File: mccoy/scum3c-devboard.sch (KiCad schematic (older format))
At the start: 26 parts, among them J1 Conn_02x10_Odd_Even, J2 Conn_02x10_Odd_Even, J3 Conn_02x05_Odd_Even, J4 Conn_01x01_Male, U9AB1 ICM-20948

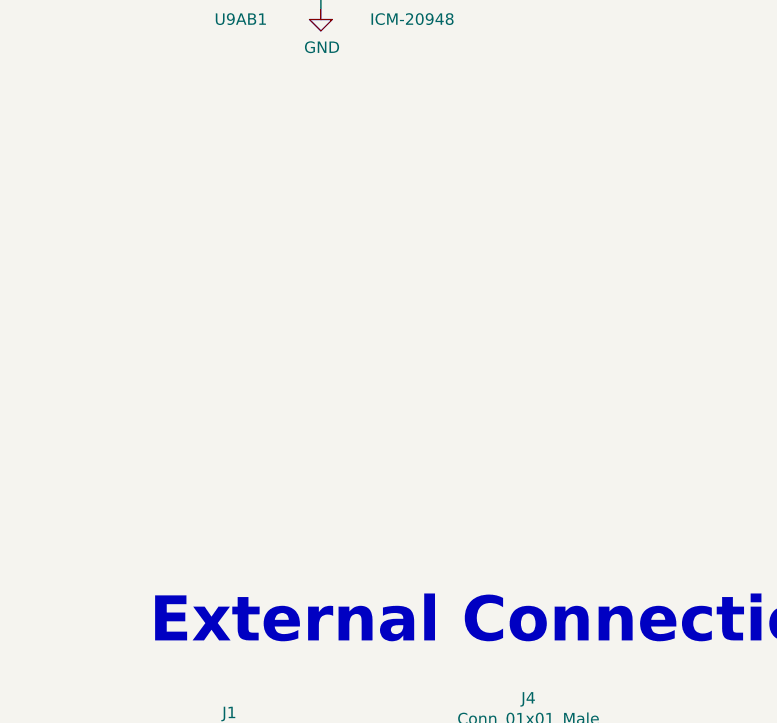
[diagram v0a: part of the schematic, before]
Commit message: assigned most footprints
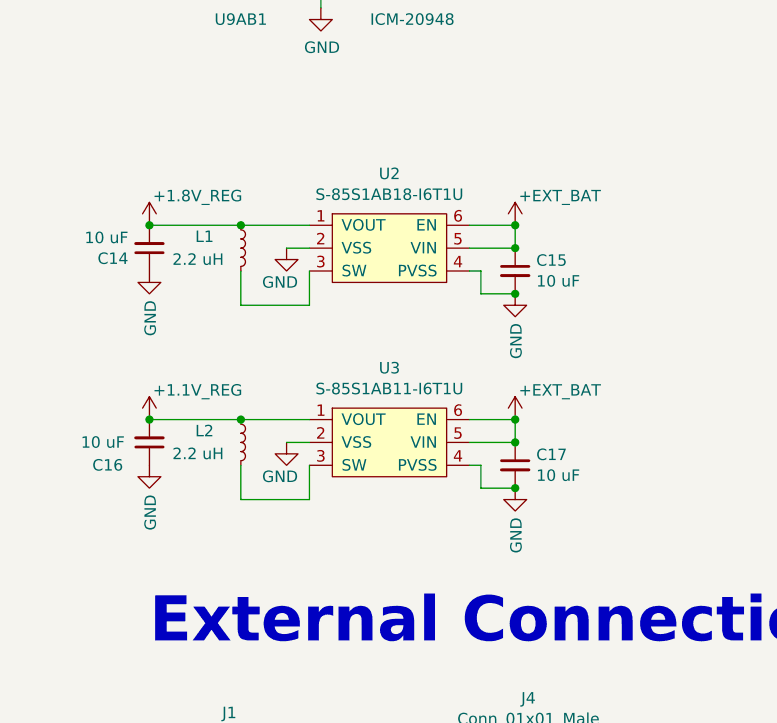
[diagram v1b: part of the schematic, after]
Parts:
- added C14, C15, C16, C17: 10 uF, symbol Device:C_Small
- added L1, L2: 2.2 uH, symbol Device:L_Small
- added U2: S-85S1AB18-I6T1U, symbol draft1library:S-85S1AB18-I6T1U
- added U3: S-85S1AB11-I6T1U, symbol draft1library:S-85S1AB11-I6T1U
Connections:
- wire segments 23 -> 47

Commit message: created snt-6a footprint
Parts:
- BT1: footprint SamacSys_Parts:2986 -> Battery:Battery_Panasonic_CR2032-VS1N_Vertical_CircularHoles
- C14, C15, C16, C17: footprint (none) -> Capacitor_SMD:C_0402_1005Metric
- J1: footprint (none) -> Connector_PinHeader_2.54mm:PinHeader_2x10_P2.54mm_Vertical
- J3: footprint (none) -> Connector_PinHeader_2.54mm:PinHeader_2x05_P2.54mm_Vertical
- L1, L2: footprint (none) -> Inductor_SMD:L_0402_1005Metric
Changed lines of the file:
@@
 F 0 "BT1" H 10000 1846 50  0000 L CNN
 F 1 "Battery_Clip" H 10000 1755 50  0000 L CNN
-F 2 "SamacSys_Parts:2986" H 9800 1750 50  0001 C CNN
+F 2 "Battery:Battery_Panasonic_CR2032-VS1N_Vertical_CircularHoles" H 9800 1750 50  0001 C CNN
 F 3 "" H 9800 1750 50  0001 C CNN
 	1    9800 1750
@@
 F 0 "J1" H 1400 7717 50  0000 C CNN
 F 1 "Conn_02x10_Odd_Even" H 1400 7626 50  0000 C CNN
-F 2 "" H 1350 7100 50  0001 C CNN
+F 2 "Connector_PinHeader_2.54mm:PinHeader_2x10_P2.54mm_Vertical" H 1350 7100 50  0001 C CNN
 F 3 "~" H 1350 7100 50  0001 C CNN
 	1    1350 7100
@@
 F 0 "J3" H 5200 7367 50  0000 C CNN
 F 1 "Conn_02x05_Odd_Even" H 5200 7276 50  0000 C CNN
-F 2 "" H 5150 6950 50  0001 C CNN
+F 2 "Connector_PinHeader_2.54mm:PinHeader_2x05_P2.54mm_Vertical" H 5150 6950 50  0001 C CNN
 F 3 "~" H 5150 6950 50  0001 C CNN
 	1    5150 6950
@@
 F 0 "C14" H 1142 4496 50  0000 L CNN
 F 1 "10 uF" H 1142 4405 50  0000 L CNN
-F 2 "" H 1050 4450 50  0001 C CNN
+F 2 "Capacitor_SMD:C_0402_1005Metric" H 1050 4450 50  0001 C CNN
 F 3 "~" H 1050 4450 50  0001 C CNN
 	1    1050 4450
@@
 F 0 "L1" H 1250 4500 50  0000 L CNN
 F 1 "2.2 uH" H 1150 4400 50  0000 L CNN
-F 2 "" H 1450 4450 50  0001 C CNN
+F 2 "Inductor_SMD:L_0402_1005Metric" H 1450 4450 50  0001 C CNN
 F 3 "~" H 1450 4450 50  0001 C CNN
 	1    1450 4450
@@
 F 0 "C16" H 1300 5400 50  0000 R CNN
 F 1 "10 uF" H 1350 5300 50  0000 R CNN
-F 2 "" H 1050 5300 50  0001 C CNN
+F 2 "Capacitor_SMD:C_0402_1005Metric" H 1050 5300 50  0001 C CNN
 F 3 "~" H 1050 5300 50  0001 C CNN
 	1    1050 5300
@@
 F 0 "L2" H 1250 5350 50  0000 L CNN
 F 1 "2.2 uH" H 1150 5250 50  0000 L CNN
-F 2 "" H 1450 5300 50  0001 C CNN
+F 2 "Inductor_SMD:L_0402_1005Metric" H 1450 5300 50  0001 C CNN
 F 3 "~" H 1450 5300 50  0001 C CNN
 	1    1450 5300
@@
 F 0 "C17" H 2742 5446 50  0000 L CNN
 F 1 "10 uF" H 2742 5355 50  0000 L CNN
-F 2 "" H 2650 5400 50  0001 C CNN
+F 2 "Capacitor_SMD:C_0402_1005Metric" H 2650 5400 50  0001 C CNN
 F 3 "~" H 2650 5400 50  0001 C CNN
 	1    2650 5400
@@
 F 0 "C15" H 2742 4596 50  0000 L CNN
 F 1 "10 uF" H 2742 4505 50  0000 L CNN
-F 2 "" H 2650 4550 50  0001 C CNN
+F 2 "Capacitor_SMD:C_0402_1005Metric" H 2650 4550 50  0001 C CNN
 F 3 "~" H 2650 4550 50  0001 C CNN
 	1    2650 4550

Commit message: added regulators to pcb
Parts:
- removed BT1: Battery_Clip, Battery:Battery_Panasonic_CR2032-VS1N_Vertical_CircularHoles, symbol draft1library:Battery_Clip
- added BT1: Battery_Cell, Battery:Battery_Panasonic_CR2032-VS1N_Vertical_CircularHoles, symbol Device:Battery_Cell
- U2, U3: footprint (none) -> SCUM:SNT-6A
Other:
- note added: "Regulators"
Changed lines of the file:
@@
 	1    0    0    -1
-$EndComp
-$Comp
-L draft1library:+VBAT #PWR047
-U 1 1 607B4D72
-P 9800 2050
-F 0 "#PWR047" H 9800 1900 50  0001 C CNN
-F 1 "+VBAT" H 9815 2223 50  0000 C CNN
-F 2 "" H 9800 2050 50  0001 C CNN
-F 3 "" H 9800 2050 50  0001 C CNN
-	1    9800 2050
-	-1   0    0    1
 $EndComp
 $Sheet
@@
 $EndSheet
 $Comp
-L draft1library:Battery_Clip BT1
-U 1 1 60775F67
-P 9800 1750
-F 0 "BT1" H 10000 1846 50  0000 L CNN
-F 1 "Battery_Clip" H 10000 1755 50  0000 L CNN
-F 2 "Battery:Battery_Panasonic_CR2032-VS1N_Vertical_CircularHoles" H 9800 1750 50  0001 C CNN
-F 3 "" H 9800 1750 50  0001 C CNN
-	1    9800 1750
-	1    0    0    -1
-$EndComp
-$Comp
 L draft1library:+VBAT #PWR048
 U 1 1 608BF8E8
-P 9850 1350
-F 0 "#PWR048" H 9850 1200 50  0001 C CNN
-F 1 "+VBAT" H 9865 1523 50  0000 C CNN
-F 2 "" H 9850 1350 50  0001 C CNN
-F 3 "" H 9850 1350 50  0001 C CNN
-	1    9850 1350
+P 9850 1650
+F 0 "#PWR048" H 9850 1500 50  0001 C CNN
+F 1 "+VBAT" H 9865 1823 50  0000 C CNN
+F 2 "" H 9850 1650 50  0001 C CNN
+F 3 "" H 9850 1650 50  0001 C CNN
+	1    9850 1650
 	1    0    0    -1
 $EndComp
@@
 L power:GND #PWR046
 U 1 1 608BFCDC
-P 9750 1350
+P 9850 2000
 AR Path="/608BFCDC" Ref="#PWR046"  Part="1"
 AR Path="/5F3B0B28/608BFCDC" Ref="#PWR?"  Part="1"
-F 0 "#PWR046" H 9750 1100 50  0001 C CNN
-F 1 "GND" H 9755 1177 50  0000 C CNN
-F 2 "" H 9750 1350 50  0001 C CNN
-F 3 "" H 9750 1350 50  0001 C CNN
-	1    9750 1350
-	-1   0    0    1
+F 0 "#PWR046" H 9850 1750 50  0001 C CNN
+F 1 "GND" H 9855 1827 50  0000 C CNN
+F 2 "" H 9850 2000 50  0001 C CNN
+F 3 "" H 9850 2000 50  0001 C CNN
+	1    9850 2000
+	1    0    0    -1
 $EndComp
 $Comp
@@
 F 0 "U3" H 2100 5625 50  0000 C CNN
 F 1 "S-85S1AB11-I6T1U" H 2100 5534 50  0000 C CNN
-F 2 "" H 2300 5200 50  0001 C CNN
+F 2 "SCUM:SNT-6A" H 2300 5200 50  0001 C CNN
 F 3 "" H 2300 5200 50  0001 C CNN
 	1    2100 5300
@@
 F 0 "U2" H 2100 4775 50  0000 C CNN
 F 1 "S-85S1AB18-I6T1U" H 2100 4684 50  0000 C CNN
-F 2 "" H 2300 4350 50  0001 C CNN
+F 2 "SCUM:SNT-6A" H 2300 4350 50  0001 C CNN
 F 3 "" H 2300 4350 50  0001 C CNN
 	1    2100 4450
@@
 	1    0    0    -1
 $EndComp
+$Comp
+L Device:Battery_Cell BT1
+U 1 1 612886A9
+P 9850 1850
+F 0 "BT1" H 9968 1946 50  0000 L CNN
+F 1 "Battery_Cell" H 9968 1855 50  0000 L CNN
+F 2 "Battery:Battery_Panasonic_CR2032-VS1N_Vertical_CircularHoles" V 9850 1910 50  0001 C CNN
+F 3 "~" V 9850 1910 50  0001 C CNN
+	1    9850 1850
+	1    0    0    -1
+$EndComp
+Text Notes 1050 4000 0    197  ~ 39
+Regulators
 $EndSCHEMATC

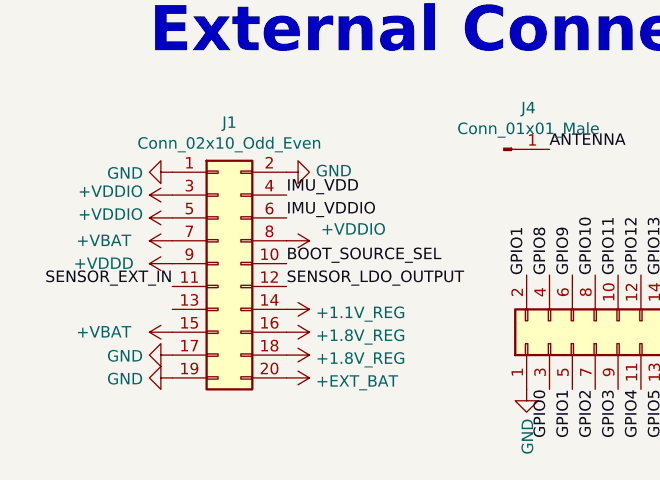
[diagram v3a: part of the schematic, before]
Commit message: moved pins for better tracing
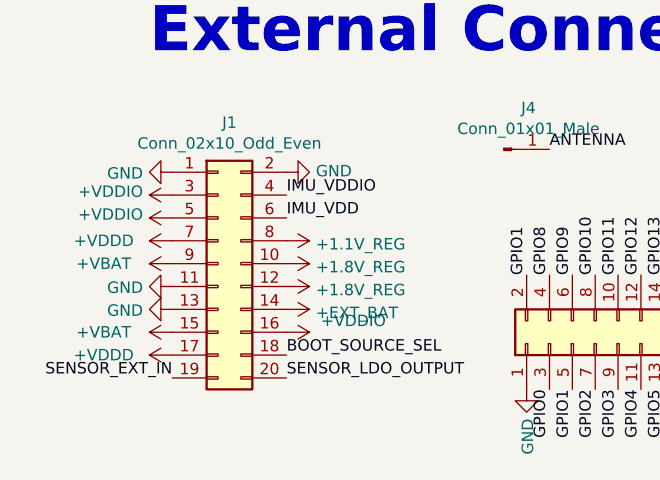
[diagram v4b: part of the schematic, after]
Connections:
- net +1.1V_REG: now also J1.8 (Pin_8); no longer J1.14 (Pin_14)
- net +1.8V_REG: now also J1.10 (Pin_10), J1.12 (Pin_12); no longer J1.16 (Pin_16), J1.18 (Pin_18)
- net +EXT_BAT: now also J1.14 (Pin_14); no longer J1.20 (Pin_20)
- net +VBAT: now also J1.9 (Pin_9); no longer J1.7 (Pin_7)
- net +VDDD: now also J1.17 (Pin_17), J1.7 (Pin_7); no longer J1.9 (Pin_9)
- net +VDDIO: now also J1.16 (Pin_16); no longer J1.8 (Pin_8)
- net BOOT_SOURCE_SEL: now also J1.18 (Pin_18); no longer J1.10 (Pin_10)
- net GND: now also J1.11 (Pin_11), J1.13 (Pin_13); no longer J1.17 (Pin_17), J1.19 (Pin_19)
- net IMU_VDD: now also J1.6 (Pin_6); no longer J1.4 (Pin_4)
- net IMU_VDDIO: now also J1.4 (Pin_4); no longer J1.6 (Pin_6)
- net SENSOR_EXT_IN: now also J1.19 (Pin_19); no longer J1.11 (Pin_11)
- net SENSOR_LDO_OUTPUT: now also J1.20 (Pin_20); no longer J1.12 (Pin_12)
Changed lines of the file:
@@
 Text Label 1700 1750 2    50   ~ 0
 IMU_VDDIO
-Text Label 1650 6900 0    50   ~ 0
+Text Label 1650 6800 0    50   ~ 0
 IMU_VDDIO
 Text Label 3200 7150 1    50   ~ 0
@@
 Text Label 3500 7150 1    50   ~ 0
 GPIO15
-Text Label 1650 6800 0    50   ~ 0
+Text Label 1650 6900 0    50   ~ 0
 IMU_VDD
 NoConn ~ 1300 2950
@@
 	0    1    1    0
 $EndComp
-Text Label 1650 7100 0    50   ~ 0
+Text Label 1650 7500 0    50   ~ 0
 BOOT_SOURCE_SEL
 Text Label 5450 7150 0    50   ~ 0
@@
 	0    1    1    0
 $EndComp
-$Comp
-L draft1library:+VDDD #PWR07
-U 1 1 60769F1D
-P 1150 7100
-F 0 "#PWR07" H 1150 6950 50  0001 C CNN
-F 1 "+VDDD" V 1150 7400 50  0000 C CNN
-F 2 "" H 1150 7100 50  0001 C CNN
-F 3 "" H 1150 7100 50  0001 C CNN
-	1    1150 7100
-	0    -1   -1   0
-$EndComp
-Text Label 1150 7200 2    50   ~ 0
+Text Label 1150 7600 2    50   ~ 0
 SENSOR_EXT_IN
-Text Label 1650 7200 0    50   ~ 0
+Text Label 1650 7600 0    50   ~ 0
 SENSOR_LDO_OUTPUT
 Text Label 4950 6950 2    50   ~ 0
@@
 L draft1library:+VBAT #PWR?
 U 1 1 6076D7B9
-P 1150 7000
+P 1150 7400
 AR Path="/5F3B1D81/6076D7B9" Ref="#PWR?"  Part="1"
 AR Path="/5F41418C/6076D7B9" Ref="#PWR?"  Part="1"
 AR Path="/5F414989/6076D7B9" Ref="#PWR?"  Part="1"
 AR Path="/6076D7B9" Ref="#PWR06"  Part="1"
-F 0 "#PWR06" H 1150 6850 50  0001 C CNN
-F 1 "+VBAT" V 1150 7300 50  0000 C CNN
-F 2 "" H 1150 7000 50  0001 C CNN
-F 3 "" H 1150 7000 50  0001 C CNN
-	1    1150 7000
+F 0 "#PWR06" H 1150 7250 50  0001 C CNN
+F 1 "+VBAT" V 1150 7700 50  0000 C CNN
+F 2 "" H 1150 7400 50  0001 C CNN
+F 3 "" H 1150 7400 50  0001 C CNN
+	1    1150 7400
 	0    -1   -1   0
 $EndComp
@@
 F 3 "" H 1150 6700 50  0001 C CNN
 	1    1150 6700
-	0    1    1    0
-$EndComp
-$Comp
-L draft1library:+VDDIO #PWR?
-U 1 1 6076E794
-P 1650 7000
-AR Path="/5F3B1D81/6076E794" Ref="#PWR?"  Part="1"
-AR Path="/6076E794" Ref="#PWR08"  Part="1"
-F 0 "#PWR08" H 1650 6850 50  0001 C CNN
-F 1 "+VDDIO" V 1600 7150 50  0000 L CNN
-F 2 "" H 1650 7000 50  0001 C CNN
-F 3 "" H 1650 7000 50  0001 C CNN
-	1    1650 7000
 	0    1    1    0
 $EndComp
@@
 L draft1library:+VBAT #PWR?
 U 1 1 6127ADAC
-P 1150 7400
+P 1150 7100
 AR Path="/5F3B1D81/6127ADAC" Ref="#PWR?"  Part="1"
 AR Path="/5F41418C/6127ADAC" Ref="#PWR?"  Part="1"
 AR Path="/5F414989/6127ADAC" Ref="#PWR?"  Part="1"
 AR Path="/6127ADAC" Ref="#PWR0107"  Part="1"
-F 0 "#PWR0107" H 1150 7250 50  0001 C CNN
-F 1 "+VBAT" V 1150 7700 50  0000 C CNN
-F 2 "" H 1150 7400 50  0001 C CNN
-F 3 "" H 1150 7400 50  0001 C CNN
-	1    1150 7400
+F 0 "#PWR0107" H 1150 6950 50  0001 C CNN
+F 1 "+VBAT" V 1150 7400 50  0000 C CNN
+F 2 "" H 1150 7100 50  0001 C CNN
+F 3 "" H 1150 7100 50  0001 C CNN
+	1    1150 7100
 	0    -1   -1   0
 $EndComp
@@
 L power:GND #PWR0108
 U 1 1 6127B18B
-P 1150 7500
-F 0 "#PWR0108" H 1150 7250 50  0001 C CNN
-F 1 "GND" V 1155 7372 50  0000 R CNN
-F 2 "" H 1150 7500 50  0001 C CNN
-F 3 "" H 1150 7500 50  0001 C CNN
-	1    1150 7500
+P 1150 7200
+F 0 "#PWR0108" H 1150 6950 50  0001 C CNN
+F 1 "GND" V 1155 7072 50  0000 R CNN
+F 2 "" H 1150 7200 50  0001 C CNN
+F 3 "" H 1150 7200 50  0001 C CNN
+	1    1150 7200
 	0    1    1    0
 $EndComp
@@
 L power:GND #PWR0109
 U 1 1 6127B4FF
-P 1150 7600
-F 0 "#PWR0109" H 1150 7350 50  0001 C CNN
-F 1 "GND" V 1155 7472 50  0000 R CNN
-F 2 "" H 1150 7600 50  0001 C CNN
-F 3 "" H 1150 7600 50  0001 C CNN
-	1    1150 7600
+P 1150 7300
+F 0 "#PWR0109" H 1150 7050 50  0001 C CNN
+F 1 "GND" V 1155 7172 50  0000 R CNN
+F 2 "" H 1150 7300 50  0001 C CNN
+F 3 "" H 1150 7300 50  0001 C CNN
+	1    1150 7300
 	0    1    1    0
 $EndComp
@@
 L draft1library:+1.1V_REG #PWR0110
 U 1 1 61280E78
+P 1650 7000
+F 0 "#PWR0110" H 1650 6850 50  0001 C CNN
+F 1 "+1.1V_REG" V 1665 7128 50  0000 L CNN
+F 2 "" H 1650 7000 50  0001 C CNN
+F 3 "" H 1650 7000 50  0001 C CNN
+	1    1650 7000
+	0    1    1    0
+$EndComp
+$Comp
+L draft1library:+1.8V_REG #PWR0111
+U 1 1 61281B91
+P 1650 7100
+F 0 "#PWR0111" H 1650 6950 50  0001 C CNN
+F 1 "+1.8V_REG" V 1665 7228 50  0000 L CNN
+F 2 "" H 1650 7100 50  0001 C CNN
+F 3 "" H 1650 7100 50  0001 C CNN
+	1    1650 7100
+	0    1    1    0
+$EndComp
+$Comp
+L draft1library:+1.8V_REG #PWR0112
+U 1 1 612829BE
+P 1650 7200
+F 0 "#PWR0112" H 1650 7050 50  0001 C CNN
+F 1 "+1.8V_REG" V 1665 7328 50  0000 L CNN
+F 2 "" H 1650 7200 50  0001 C CNN
+F 3 "" H 1650 7200 50  0001 C CNN
+	1    1650 7200
+	0    1    1    0
+$EndComp
+$Comp
+L draft1library:+EXT_BAT #PWR0113
+U 1 1 612835E6
 P 1650 7300
-F 0 "#PWR0110" H 1650 7150 50  0001 C CNN
-F 1 "+1.1V_REG" V 1665 7428 50  0000 L CNN
+F 0 "#PWR0113" H 1650 7150 50  0001 C CNN
+F 1 "+EXT_BAT" V 1665 7428 50  0000 L CNN
 F 2 "" H 1650 7300 50  0001 C CNN
 F 3 "" H 1650 7300 50  0001 C CNN
 	1    1650 7300
-	0    1    1    0
-$EndComp
-$Comp
-L draft1library:+1.8V_REG #PWR0111
-U 1 1 61281B91
-P 1650 7400
-F 0 "#PWR0111" H 1650 7250 50  0001 C CNN
-F 1 "+1.8V_REG" V 1665 7528 50  0000 L CNN
-F 2 "" H 1650 7400 50  0001 C CNN
-F 3 "" H 1650 7400 50  0001 C CNN
-	1    1650 7400
-	0    1    1    0
-$EndComp
-$Comp
-L draft1library:+1.8V_REG #PWR0112
-U 1 1 612829BE
-P 1650 7500
-F 0 "#PWR0112" H 1650 7350 50  0001 C CNN
-F 1 "+1.8V_REG" V 1665 7628 50  0000 L CNN
-F 2 "" H 1650 7500 50  0001 C CNN
-F 3 "" H 1650 7500 50  0001 C CNN
-	1    1650 7500
-	0    1    1    0
-$EndComp
-$Comp
-L draft1library:+EXT_BAT #PWR0113
-U 1 1 612835E6
-P 1650 7600
-F 0 "#PWR0113" H 1650 7450 50  0001 C CNN
-F 1 "+EXT_BAT" V 1665 7728 50  0000 L CNN
-F 2 "" H 1650 7600 50  0001 C CNN
-F 3 "" H 1650 7600 50  0001 C CNN
-	1    1650 7600
 	0    1    1    0
 $EndComp
@@
 Text Notes 1050 4000 0    197  ~ 39
 Regulators
+$Comp
+L draft1library:+VDDD #PWR0125
+U 1 1 612C7D86
+P 1150 7000
+F 0 "#PWR0125" H 1150 6850 50  0001 C CNN
+F 1 "+VDDD" V 1150 7300 50  0000 C CNN
+F 2 "" H 1150 7000 50  0001 C CNN
+F 3 "" H 1150 7000 50  0001 C CNN
+	1    1150 7000
+	0    -1   -1   0
+$EndComp
+$Comp
+L draft1library:+VDDIO #PWR?
+U 1 1 6076E794
+P 1650 7400
+AR Path="/5F3B1D81/6076E794" Ref="#PWR?"  Part="1"
+AR Path="/6076E794" Ref="#PWR08"  Part="1"
+F 0 "#PWR08" H 1650 7250 50  0001 C CNN
+F 1 "+VDDIO" V 1600 7550 50  0000 L CNN
+F 2 "" H 1650 7400 50  0001 C CNN
+F 3 "" H 1650 7400 50  0001 C CNN
+	1    1650 7400
+	0    1    1    0
+$EndComp
+$Comp
+L draft1library:+VDDD #PWR07
+U 1 1 60769F1D
+P 1150 7500
+F 0 "#PWR07" H 1150 7350 50  0001 C CNN
+F 1 "+VDDD" V 1150 7800 50  0000 C CNN
+F 2 "" H 1150 7500 50  0001 C CNN
+F 3 "" H 1150 7500 50  0001 C CNN
+	1    1150 7500
+	0    -1   -1   0
+$EndComp
 $EndSCHEMATC
